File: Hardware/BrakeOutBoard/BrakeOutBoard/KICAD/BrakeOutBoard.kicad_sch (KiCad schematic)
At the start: 52 parts, among them J1 To USB converter, J10 WhiperWater, J11 BrakePads, J12 BrakeFluid, J13 Door_R, J14 OilPresure, J15 Door_S, J16 TFT_CS, J17 TFT_DC, J18 TFT_GND, J19 TFT_SLK, J2 K15, J20 Conn_01x19_Socket, J21 TFT_MOSI, J22 TFT_RST, J24 Reset, J25 Can_H, J26 Memory, J27 Can_L, J28 Trunk, J29 Mode, J3 K30, J4 TFT_5V, J5 Conn_01x19_Socket, J6 K31, J7 Coolant, J8 oilSensor, J9 MotorCap, Q1 MMDT3904, Q2 LBSS84LT1G, U1 LTV-847, U101 SN65HVD230DR, U2 LTV-847, U3 LVT 817, U4 LTV-847

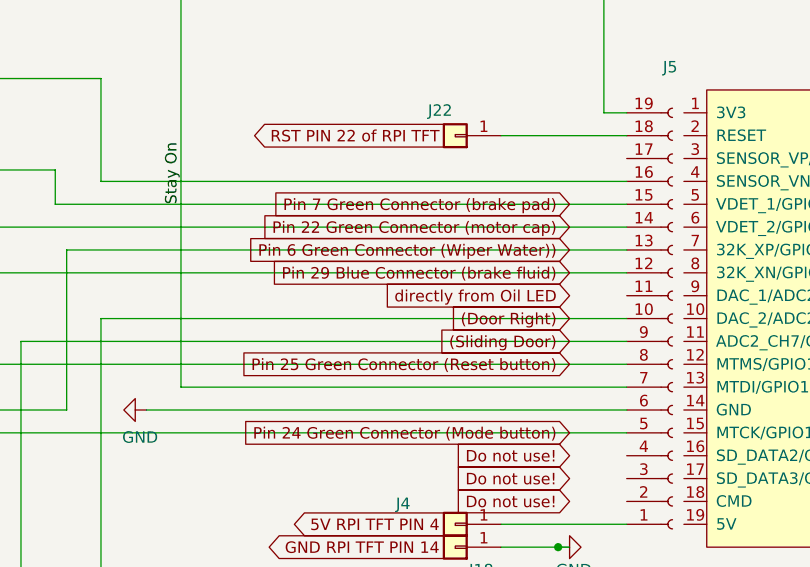
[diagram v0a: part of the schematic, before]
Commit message: Add files via upload
Forgot to include connector for Oil Level LED
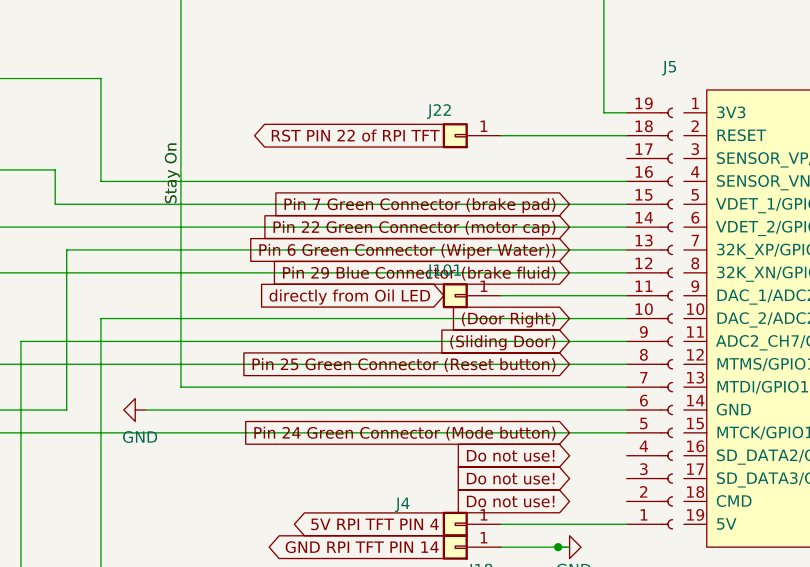
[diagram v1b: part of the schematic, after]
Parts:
- added J101: O_Lev_LED, Connector_Wire:SolderWire-0.5sqmm_1x01_D0.9mm_OD2.1mm, symbol Connector_Generic:Conn_01x01
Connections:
- net at J5.11 (Pin_11): now also J101.1 (Pin_1)
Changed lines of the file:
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@@
 	(wire
 		(pts
+			(xy 265.43 91.44) (xy 279.4 91.44)
+		)
+		(stroke
+			(width 0)
+			(type default)
+		)
+	)
+	(wire
+		(pts
 			(xy 39.37 113.03) (xy 68.58 113.03)
 		)
@@
 	(global_label "directly from Oil LED"
 		(shape input)
-		(at 273.05 91.44 180)
+		(at 259.08 91.44 180)
 		(fields_autoplaced yes)
 		(effects
@@
 		)
 		(property "Intersheetrefs" "${INTERSHEET_REFS}"
-			(at 249.6845 91.44 0)
+			(at 235.7145 91.44 0)
 			(effects
 				(font
@@
 					(unit 1)
 				)
+			)
+		)
+	)
+	(symbol
+		(lib_id "Connector_Generic:Conn_01x01")
+		(at 260.35 91.44 180)
+		(unit 1)
+		(exclude_from_sim no)
+		(in_bom yes)
+		(on_board yes)
+		(dnp no)
+		(property "Reference" "J101"
+			(at 257.302 88.646 0)
+			(effects
+				(font
+					(size 1.27 1.27)
+				)
+				(justify right)
+			)
+		)
+		(property "Value" "O_Lev_LED"
+			(at 261.6199 88.9 90)
+			(effects
+				(font
+					(size 1.27 1.27)
+				)
+				(justify right)
+				(hide yes)
+			)
+		)
+		(property "Footprint" "Connector_Wire:SolderWire-0.5sqmm_1x01_D0.9mm_OD2.1mm"
+			(at 260.35 91.44 0)
+			(effects
+				(font
+					(size 1.27 1.27)
+				)
+				(hide yes)
+			)
+		)
+		(property "Datasheet" "~"
+			(at 260.35 91.44 0)
+			(effects
+				(font
+					(size 1.27 1.27)
+				)
+				(hide yes)
+			)
+		)
+		(property "Description" "Generic connector, single row, 01x01, script generated (kicad-library-utils/schlib/autogen/connector/)"
+			(at 260.35 91.44 0)
+			(effects
+				(font
+					(size 1.27 1.27)
+				)
+				(hide yes)
+			)
+		)
+		(pin "1"
+		)
+		(instances
+			(project "BrakeOutBoard"
+				(path "/c67af5fc-5bb1-4753-93c7-831b7a5a7d41"
+					(reference "J101")
+					(unit 1)
+				)
